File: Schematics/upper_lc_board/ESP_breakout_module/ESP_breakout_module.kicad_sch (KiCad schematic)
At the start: 22 parts, among them U1 ESP32-S3-WROOM-1-N16R2, U2 CAN_T_SN65HVD230DR, U3 PD_D3V3XA4B10LP

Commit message: 2nd temp commit for new ADC circuitry
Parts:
- added D13: FAULT_LED, LED_SMD:LED_1206_3216Metric, symbol Device:LED
- added R27: 330, Capacitor_SMD:C_0402_1005Metric, symbol Device:R
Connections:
- net GND: now also D13.2 (A)
- net GPIO_11: now also U1.20 (IO12), R27.1
- net GPIO_13: now also U1.21 (IO13)
- net GPIO_14: now reaches U1.22 (IO14)
- new net: D13.1 (K), R27.2

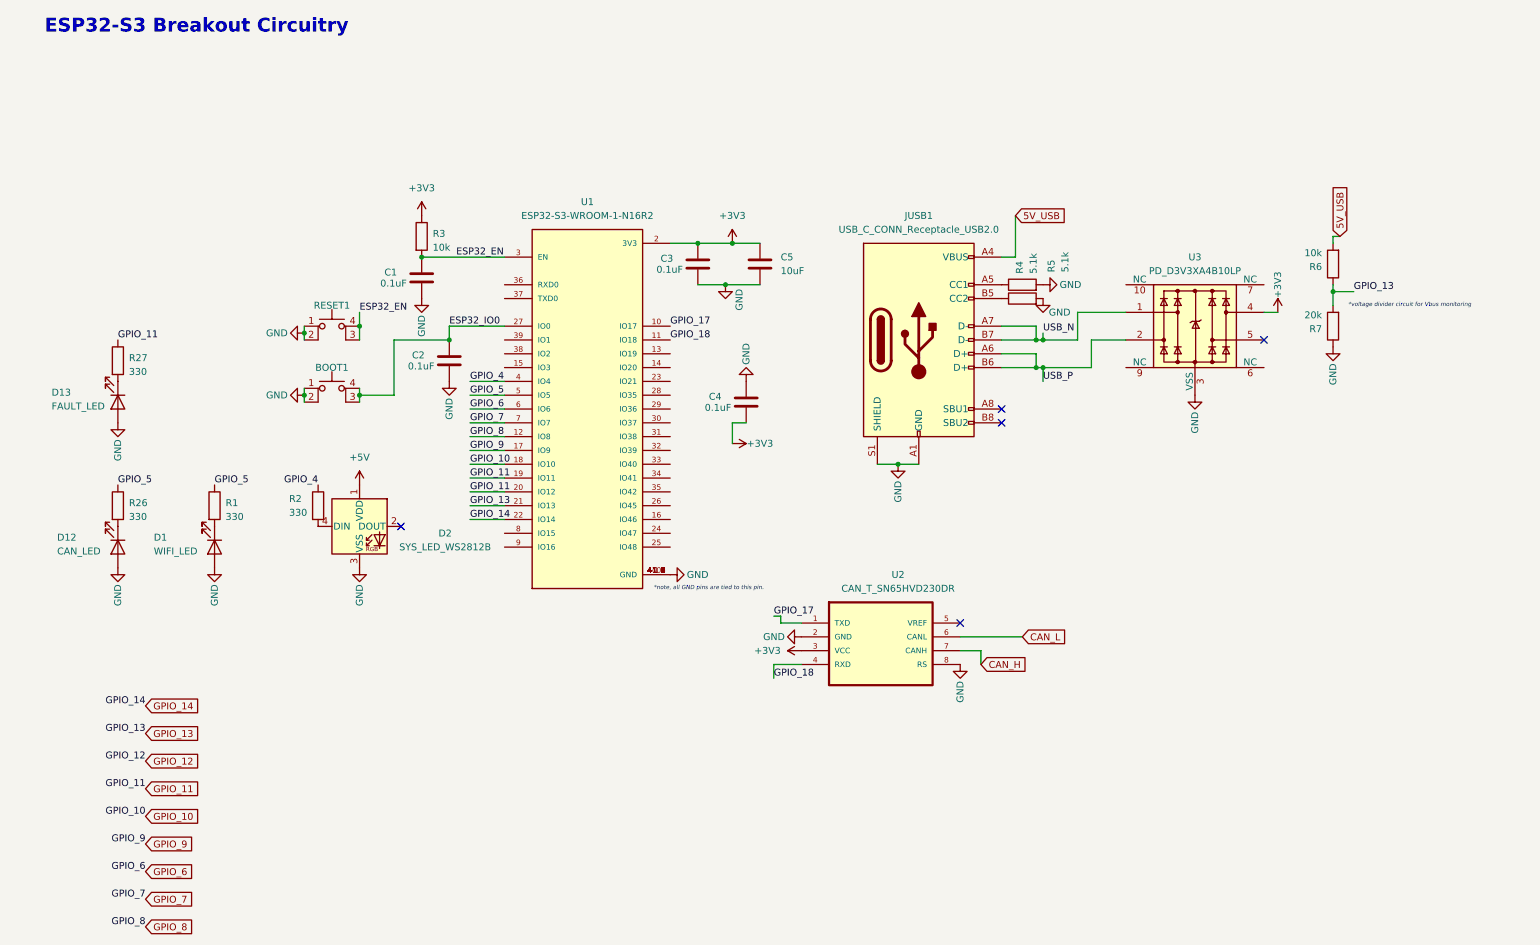
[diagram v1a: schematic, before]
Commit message: start redesigning ADC circuitry, organize schematic files. adding OPAMPS for buffered voltage divider on HALL & on PTs. layout to be adjusted after.
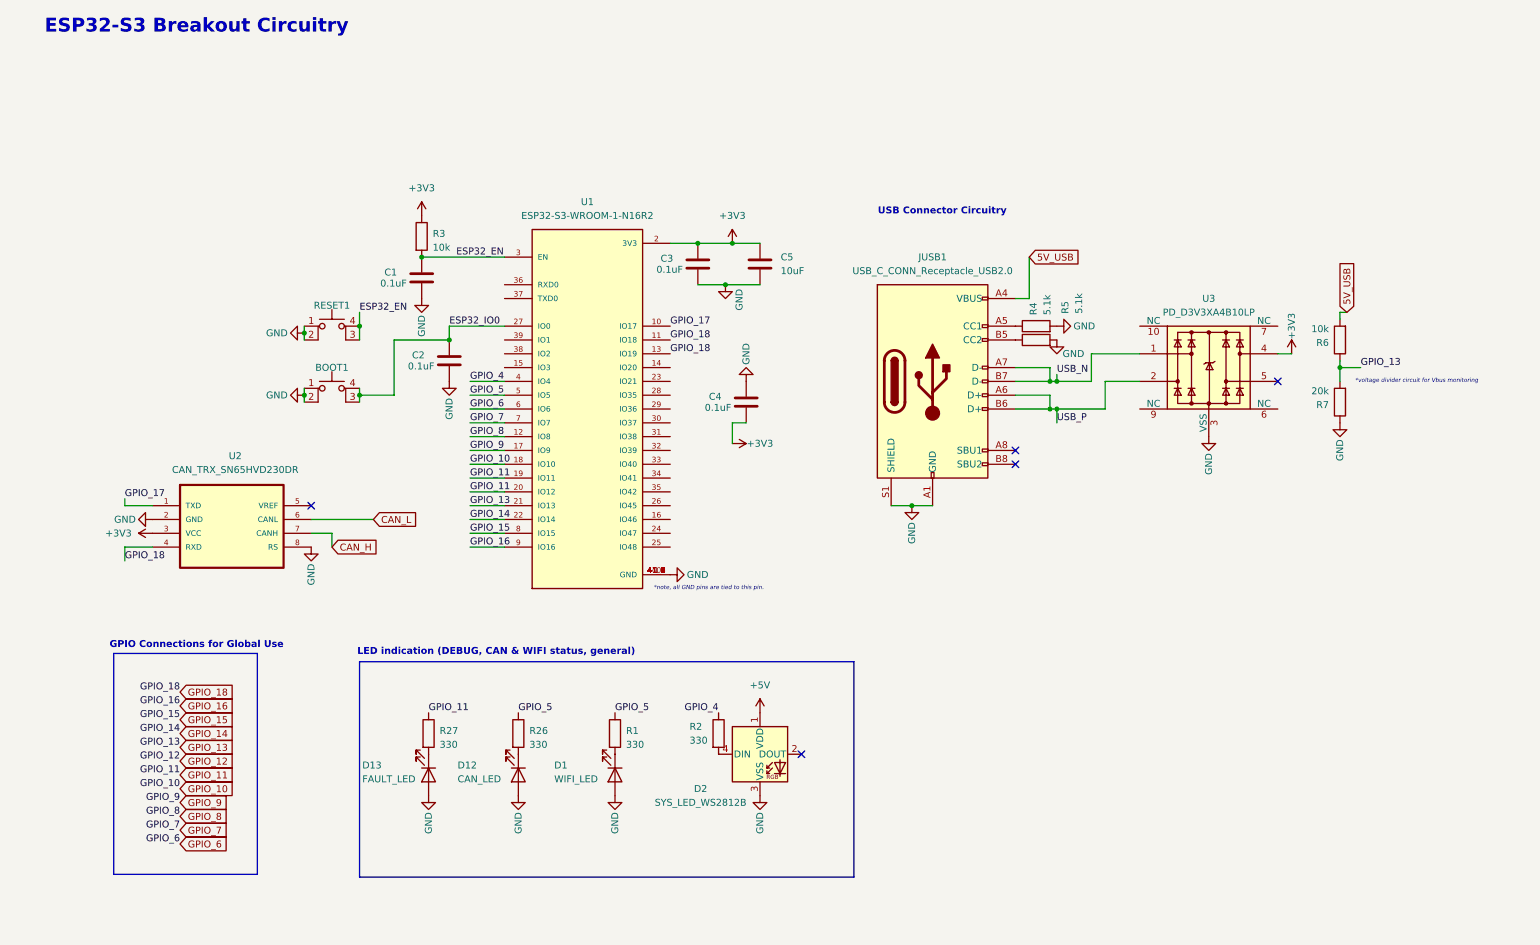
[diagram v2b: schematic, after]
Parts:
- U2: value CAN_T_SN65HVD230DR -> CAN_TRX_SN65HVD230DR
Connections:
- net GPIO_18: now also U1.13 (IO19)
- net GPIO_15: now reaches U1.8 (IO15)
- net GPIO_16: now reaches U1.9 (IO16)
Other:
- note added: "GPIO Connections for Global Use"
- note added: "LED indication (DEBUG, CAN & WIFI status, general)"
- note added: "USB Connector Circuitry"
- moved on the sheet: D1, D12, D13, D2, JUSB1, R1, R2, R26, R27, R4, R5, R6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

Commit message: breakout circuitry review
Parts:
- added C27: 0.1uF, Capacitor_SMD:C_0603_1608Metric, symbol Device:C
- added C28: 10nF, Capacitor_SMD:C_0603_1608Metric, symbol Device:C
- added R40, R41: 60, Capacitor_SMD:C_0402_1005Metric, symbol Device:R
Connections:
- net CAN_H: now also R41.1
- net CAN_L: now also R40.2
- net GND: now also C27.1
- net GPIO_11: no longer U1.20 (IO12)
- net GPIO_12: now also U1.20 (IO12)
- net GPIO_13: no longer R6.1, R7.2
- net GPIO_18: no longer U1.13 (IO19)
- net USB_N: now also U1.13 (IO19)
- net USB_P: now also U1.14 (IO20)
- net at U2.5 (VREF): now also C28.1
- net GPIO_3: now reaches U1.15 (IO3)
- net GPIO_46: now reaches U1.16 (IO46)
- net GPIO_21: now reaches U1.23 (IO21)
- net GPIO_21: now also R6.1, R7.2
- net GPIO_47: now reaches U1.24 (IO47)
- net GPIO_48: now reaches U1.25 (IO48)
- net GPIO_45: now reaches U1.26 (IO45)
- net GPIO_35: now reaches U1.28 (IO35)
- net GPIO_36: now reaches U1.29 (IO36)
- net GPIO_37: now reaches U1.30 (IO37)
- net GPIO_38: now reaches U1.31 (IO38)
- net GPIO_39: now reaches U1.32 (IO39)
- net GPIO_40: now reaches U1.33 (IO40)
- net GPIO_41: now reaches U1.34 (IO41)
- net GPIO_42: now reaches U1.35 (IO42)
- net RX_DO: now reaches U1.36 (RXD0)
- net TX_DO: now reaches U1.37 (TXD0)
- net GPIO_2: now reaches U1.38 (IO2)
- net GPIO_1: now reaches U1.39 (IO1)
- new net: C27.2, C28.2, R40.1, R41.2
- no-connect marks 5 -> 4
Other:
- moved on the sheet: BOOT1, C4, RESET1, U2

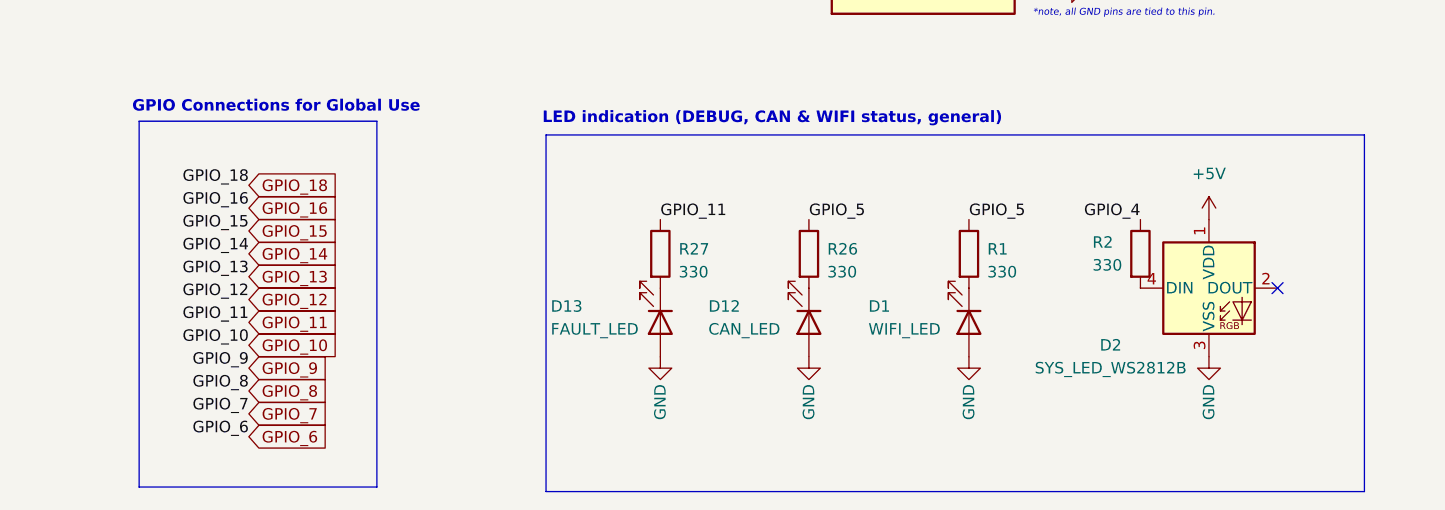
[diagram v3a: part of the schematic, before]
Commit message: add TC circuitry; finish layout next.
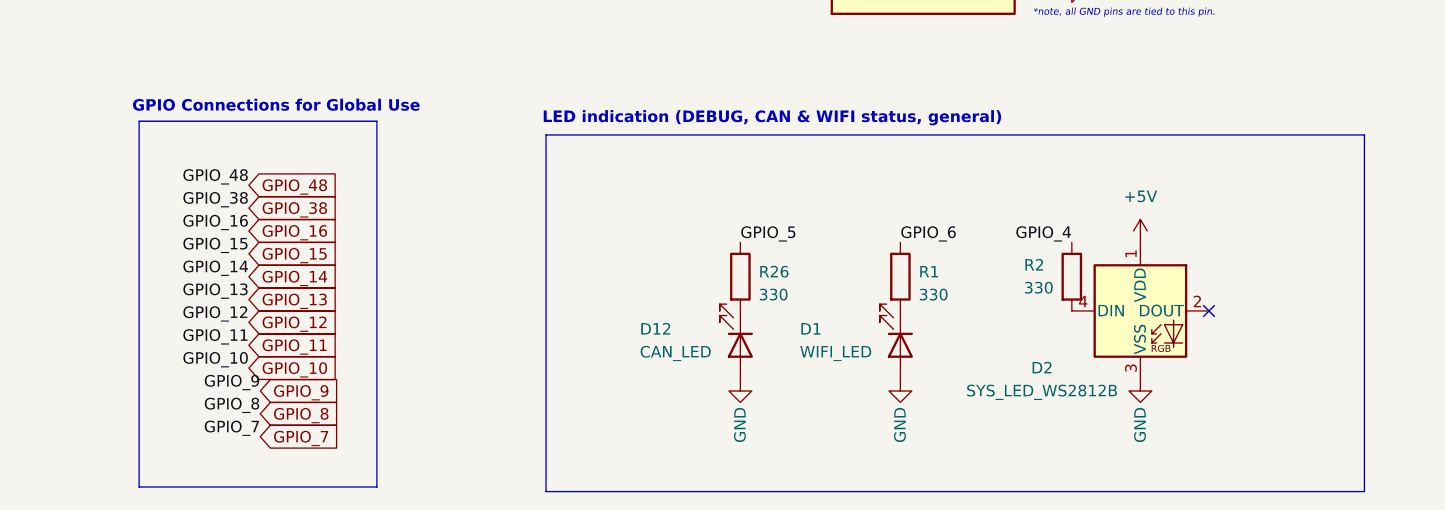
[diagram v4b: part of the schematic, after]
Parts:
- removed D13: FAULT_LED, LED_SMD:LED_1206_3216Metric, symbol Device:LED
- removed R27: 330, Capacitor_SMD:C_0402_1005Metric, symbol Device:R
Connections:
- net GPIO_5: no longer R1.1
- net GPIO_6: now also R1.1
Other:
- moved on the sheet: D1, D12, D2, R1, R2, R26

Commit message: temp commit for layout work
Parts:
- R1, R2, R26, R3, R4, R40, R41, R5, R6, R7: footprint Capacitor_SMD:C_0402_1005Metric -> Resistor_SMD:R_0402_1005Metric
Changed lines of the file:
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@@
 			)
 		)
-		(property "Footprint" "Capacitor_SMD:C_0402_1005Metric"
+		(property "Footprint" "Resistor_SMD:R_0402_1005Metric"
 			(at 255.778 88.9 90)
 			(effects
@@
 			)
 		)
-		(property "Footprint" "Capacitor_SMD:C_0402_1005Metric"
+		(property "Footprint" "Resistor_SMD:R_0402_1005Metric"
 			(at 248.158 138.43 90)
 			(effects
@@
 			)
 		)
-		(property "Footprint" "Capacitor_SMD:C_0402_1005Metric"
+		(property "Footprint" "Resistor_SMD:R_0402_1005Metric"
 			(at 130.302 152.4 90)
 			(effects
@@
 			)
 		)
-		(property "Footprint" "Capacitor_SMD:C_0402_1005Metric"
+		(property "Footprint" "Resistor_SMD:R_0402_1005Metric"
 			(at 255.778 77.47 90)
 			(effects
@@
 			)
 		)
-		(property "Footprint" "Capacitor_SMD:C_0402_1005Metric"
+		(property "Footprint" "Resistor_SMD:R_0402_1005Metric"
 			(at 111.252 152.4 90)
 			(effects
@@
 			)
 		)
-		(property "Footprint" "Capacitor_SMD:C_0402_1005Metric"
+		(property "Footprint" "Resistor_SMD:R_0402_1005Metric"
 			(at 93.472 152.4 90)
 			(effects
@@
 			)
 		)
-		(property "Footprint" "Capacitor_SMD:C_0402_1005Metric"
+		(property "Footprint" "Resistor_SMD:R_0402_1005Metric"
 			(at 83.312 58.42 90)
 			(effects
@@
 			)
 		)
-		(property "Footprint" "Capacitor_SMD:C_0402_1005Metric"
+		(property "Footprint" "Resistor_SMD:R_0402_1005Metric"
 			(at 198.12 76.708 90)
 			(effects
@@
 			)
 		)
-		(property "Footprint" "Capacitor_SMD:C_0402_1005Metric"
+		(property "Footprint" "Resistor_SMD:R_0402_1005Metric"
 			(at 198.12 79.248 90)
 			(effects
@@
 			)
 		)
-		(property "Footprint" "Capacitor_SMD:C_0402_1005Metric"
+		(property "Footprint" "Resistor_SMD:R_0402_1005Metric"
 			(at 248.158 127 90)
 			(effects

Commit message: fix footprint designators
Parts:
- BOOT1: value ~ -> BOOT
- RESET1: value ~ -> Reset
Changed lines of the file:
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@@
 			)
 		)
-		(property "Value" "~"
+		(property "Value" "BOOT"
 			(at 63.5 82.55 0)
 			(effects
@@
 					(size 1.27 1.27)
 				)
+				(hide yes)
 			)
 		)
@@
 			)
 		)
-		(property "Value" "~"
+		(property "Value" "Reset"
 			(at 63.5 71.12 0)
 			(effects
@@
 					(size 1.27 1.27)
 				)
+				(hide yes)
 			)
 		)

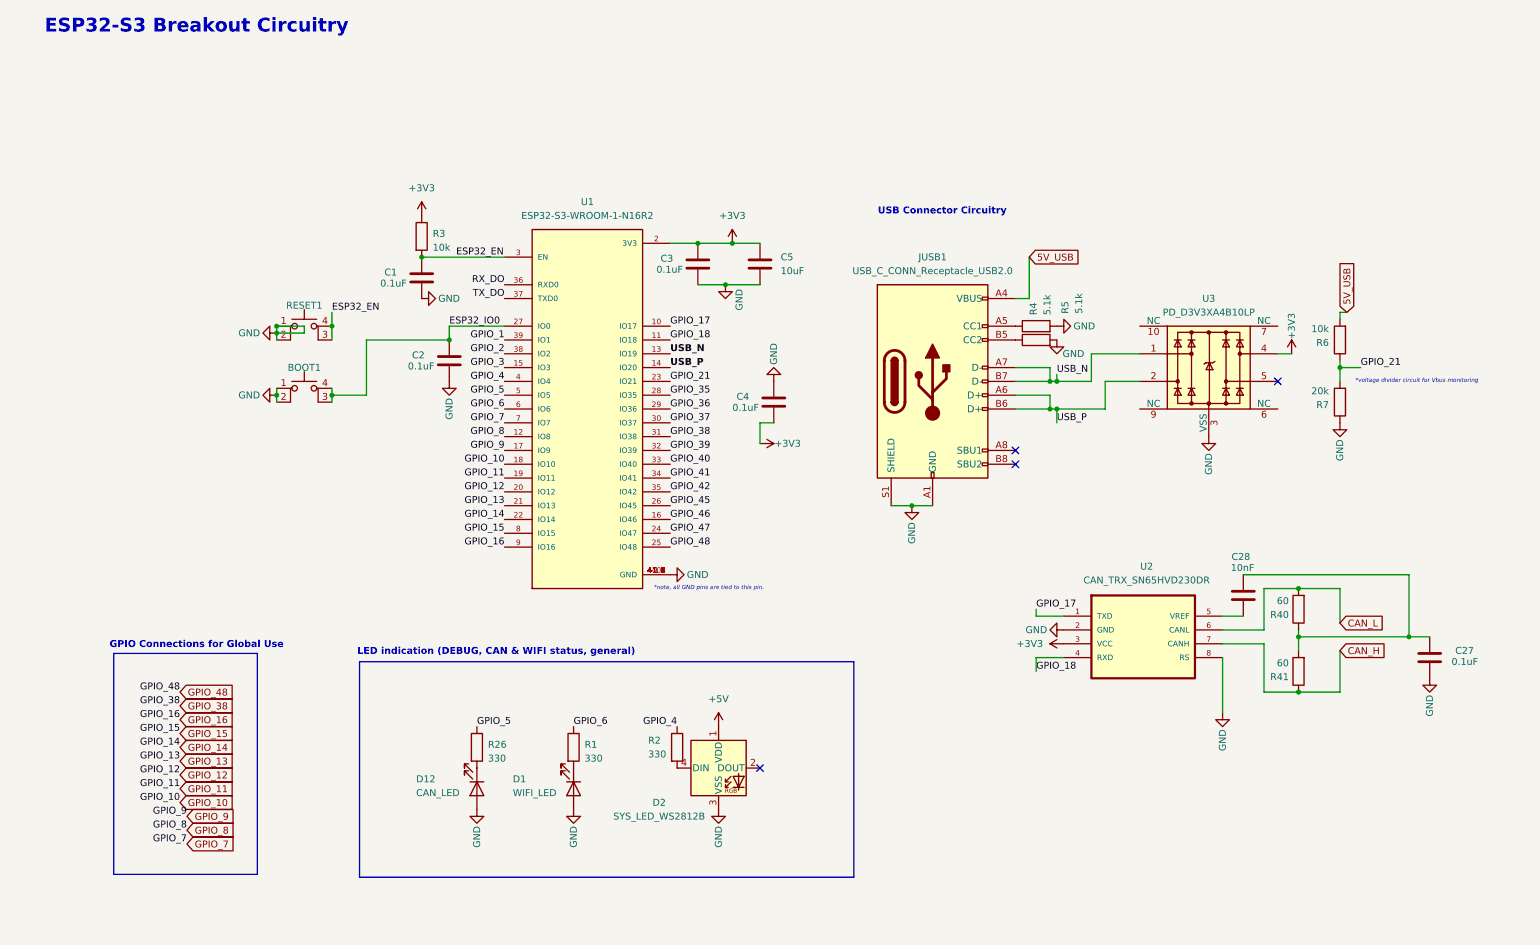
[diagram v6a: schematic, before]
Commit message: revise & organize some circuitry, next: replace MUX with ideal diodes, finish layout, rename GPIO labels for clarity
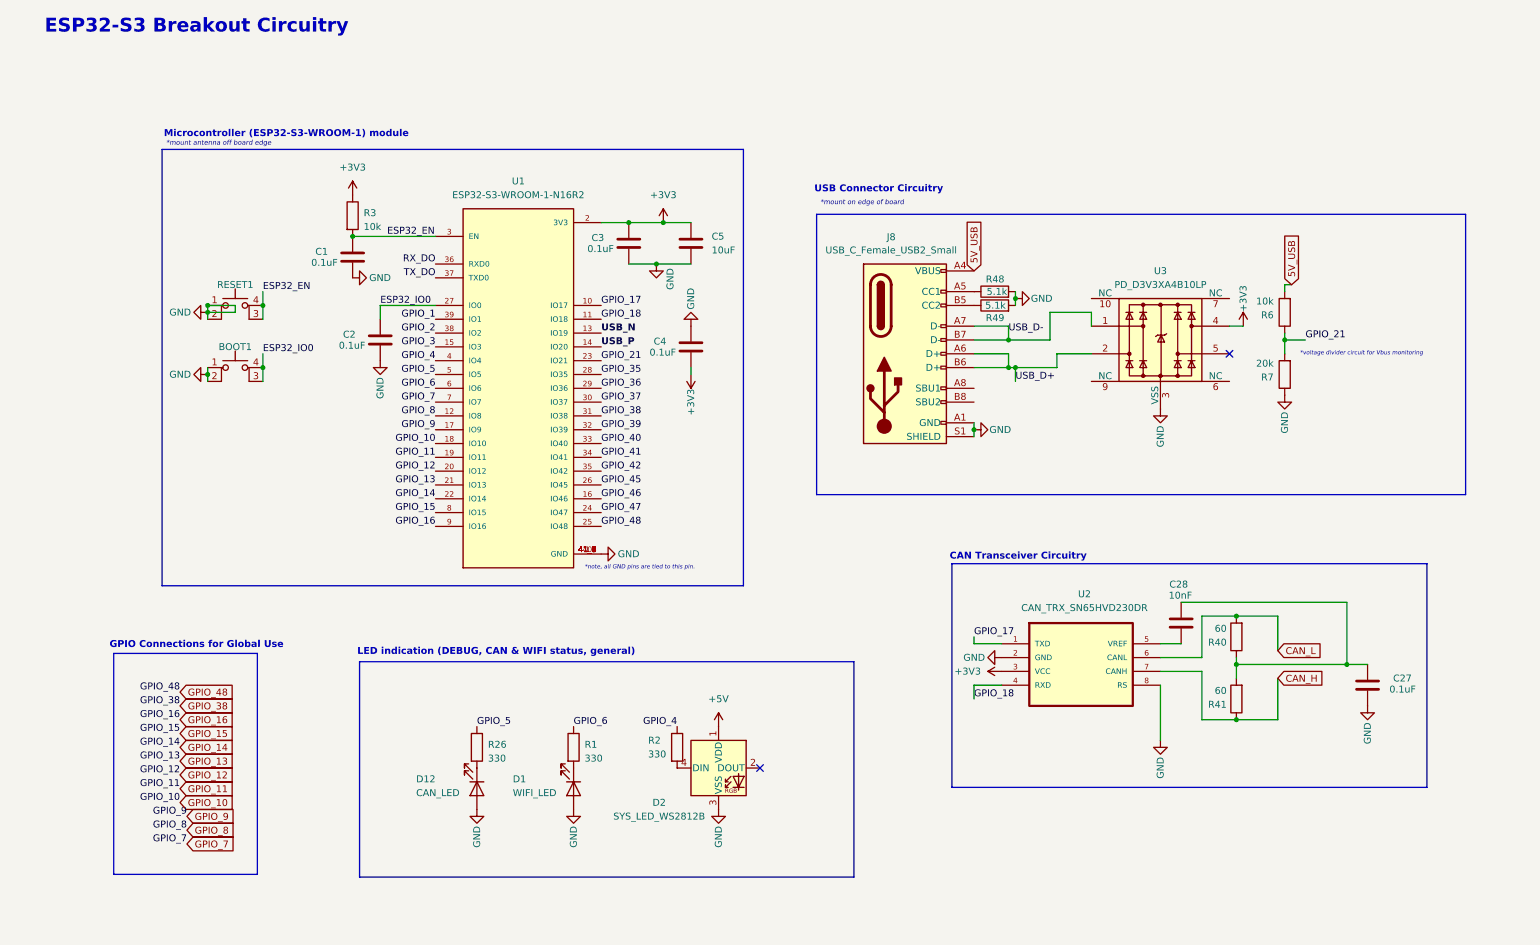
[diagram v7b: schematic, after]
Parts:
- removed JUSB1: USB_C_CONN_Receptacle_USB2.0, Connector_USB:USB_C_Receptacle_GCT_USB4105-xx-A_16P_TopMnt_Horizontal, symbol Connector:USB_C_Receptacle_USB2.0
- removed R4, R5: 5.1k, Resistor_SMD:R_0402_1005Metric, symbol Device:R
- added J8: USB_C_Female_USB2_Small, USBC-CONN:USB_C_DB-108PWB, symbol USB_C:USB_C_Female_USB2_Small
- added R48, R49: 5.1k, Resistor_SMD:R_0402_1005Metric, symbol Device:R
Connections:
- net 5V_USB: now also J8.A4 (VBUS), J8.A9 (VBUS), J8.B4 (VBUS), J8.B9 (VBUS)
- net GND: now also J8.A1 (GND), J8.A12 (GND), J8.B1 (GND), J8.B12 (GND), J8.S1 (SHIELD), R48.2, R49.2
- net USB_N: no longer U3.1
- net USB_P: no longer U3.2
- new net: J8.B5 (CC2), R49.1
- new net: J8.A5 (CC1), R48.1
- new net USB_D+: J8.A6 (D+), J8.B6 (D+), U3.2
- new net USB_D-: J8.A7 (D-), J8.B7 (D-), U3.1
- no-connect marks 4 -> 2
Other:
- note added: "*mount antenna off board edge"
- note added: "*mount on edge of board"
- note added: "CAN Transceiver Circuitry"
- note added: "Microcontroller (ESP32-S3-WROOM-1) module"
- moved on the sheet: BOOT1, C1, C2, C27, C28, C3, C4, C5, R3, R40, R41, R6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
